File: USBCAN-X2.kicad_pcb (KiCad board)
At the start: 2 copper layers, 73 x 40.5 mm, 29 parts, among them J1 USB_B, J2 Screw_Terminal_01x08, J3 Conn_01x02_Pin, J4 Conn_02x05_Odd_Even, J5 Conn_01x02_Pin, J6 Conn_01x02_Pin, U1 STM32G491CETx, U2 LM2936-3.3, U3 MCP2542FDxMF, U4 MCP2542FDxMF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

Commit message: Update
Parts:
- added D3: LED, LED_SMD:LED_0603_1608Metric, F.Cu at (167.5, 119.1)
- added R7: 330, Resistor_SMD:R_0603_1608Metric, F.Cu at (163.0, 113.5)
- U2: footprint Package_TO_SOT_SMD:TO-252-3_TabPin2 -> Package_TO_SOT_SMD:SOT-223-3_TabPin2
- U3, U4: footprint Package_DFN_QFN:DFN-8-1EP_3x3mm_P0.65mm_EP1.55x2.4mm -> Package_SO:SOIC-8-1EP_3.9x4.9mm_P1.27mm_EP2.29x3mm
- moved J5 16.0 mm to (173.2, 107.5)
- moved J6 15.0 mm to (173.3, 99.5)
- moved J4 12.8 mm to (135.8, 119.8)
- moved R2 12.0 mm to (157.3, 113.5), turned to 0 degrees
- moved R5 11.8 mm to (178.8, 103.3)
- moved R1 11.7 mm to (148.0, 113.5), turned to 180 degrees
- moved D2 10.1 mm to (157.5, 119.0)
- moved J3 10.1 mm to (141.8, 112.4), turned to 90 degrees
- moved C2 9.78 mm to (145.8, 96.0)
- moved C1 9.55 mm to (143.3, 106.0)
- moved C10 9.02 mm to (159.8, 100.0)
- moved C3 9.02 mm to (157.8, 106.5)
- moved C4 9.02 mm to (149.8, 96.0)
- moved C7 9.02 mm to (152.8, 110.5)
- moved J1 9.02 mm to (137.1, 106.2)
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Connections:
- U1 pad 10: unconnected-(U1-PA2-Pad10) -> /LED_PA2
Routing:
- net GND: track 0.00 -> 244.7 mm, vias 0 -> 1
- net 3.3V: track 0.00 -> 154.4 mm, vias 0 -> 5
- net 5V: track 0.00 -> 79.7 mm, vias 0 -> 3
- net CAN1_RX: track 0.00 -> 62.3 mm, vias 0 -> 1
- net CAN2_P: track 63.2 -> 15.6 mm
- net CAN2_RX: track 0.00 -> 41.4 mm, vias 0 -> 2
- net SWDCLK: track 0.00 -> 33.6 mm
- net CAN2_TX: track 0.00 -> 32.9 mm, vias 0 -> 2
- net CAN1_TX: track 0.00 -> 32.1 mm, vias 0 -> 2
- net SWDIO: track 0.00 -> 29.8 mm, vias 0 -> 2
- net /LED_PA0: track 0.00 -> 22.8 mm, vias 0 -> 2
- net CAN2_N: track 34.3 -> 14.4 mm
- net Net-(J2-Pin_4): track 34.4 -> 14.8 mm
- net /LED_PA2: track 0.00 -> 18.7 mm, vias 0 -> 2
- net /LED_PA1: track 0.00 -> 13.9 mm, vias 0 -> 2
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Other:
- board size 73 x 40.5 mm -> 65 x 40 mm
- board text added: "USBCAN-X2"

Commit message: Update
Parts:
- C10, C9: value 0.1uF -> 18pF
- C5: value 10uF -> 15uF
- C6, C8: value C -> 0.1uF
- D1: value LED -> LED Green
- D2: value LED -> LED Blue
- D3: value LED -> LED Red
- J4: footprint Samtect:CON10_2X5_DUK_FTSH_SAI -> Samtect:CON10_2X5_DUK_FTSH_SAI-M
- Y1: value Crystal_Small -> 25MHz
- moved C6 1.40 mm to (166.1, 94.9)
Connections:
- U1 pad 33: USB_M -> USB_N
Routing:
- net GND: track 244.7 -> 228.2 mm, vias 1 -> 6
- net USB_N: track 0.00 -> 12.3 mm
- net CAN2_N: track 14.4 -> 24.3 mm, vias 0 -> 1
- net 5V: track 79.7 -> 76.0 mm
- net CAN1_N: track 28.6 -> 26.6 mm
- net SWDIO: track 29.8 -> 31.3 mm
- net 3.3V: track 154.4 -> 155.8 mm
- net CAN1_P: track 25.5 -> 26.1 mm
- net Net-(J2-Pin_8): track 25.2 -> 25.8 mm
- net USB_P: track 11.8 -> 12.3 mm
- added copper zone on B.Cu, net GND
- added copper zone on F.Cu, net GND

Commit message: Created PDF's
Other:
- board text added: "REV 1"
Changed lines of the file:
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@@
 		(tags "USB B receptacle horizontal through-hole")
 		(property "Reference" "J1"
-			(at 14.7875 -6.25 0)
+			(at 9.3875 -6.25 0)
 			(layer "F.SilkS")
 			(effects
@@
 		)
 	)
+	(gr_text "REV 1"
+		(at 180.2 88.8 0)
+		(layer "F.Cu")
+		(effects
+			(font
+				(size 1 1)
+				(thickness 0.15)
+			)
+			(justify left bottom)
+		)
+	)
 	(dimension
 		(type orthogonal)
@@
 		(name "GND")
 		(hatch edge 0.5)
+		(priority 1)
 		(connect_pads
 			(clearance 0.5)
@@
 		(name "GND")
 		(hatch edge 0.5)
-		(priority 1)
 		(connect_pads
 			(clearance 0.5)

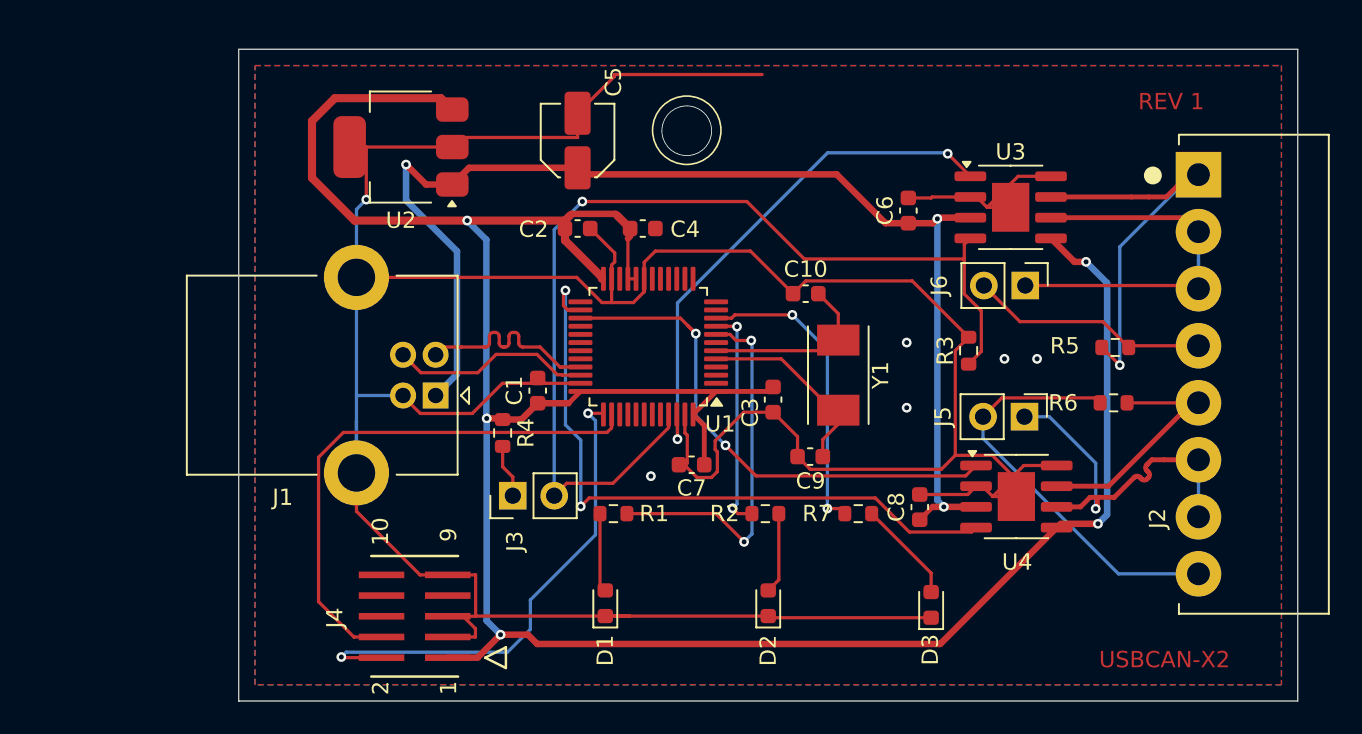
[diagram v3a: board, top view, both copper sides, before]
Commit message: Moved CAN transceiver and jumper pins. Rerouted tracks. Added 3D models to 3D folder as they are linked and not embedded.
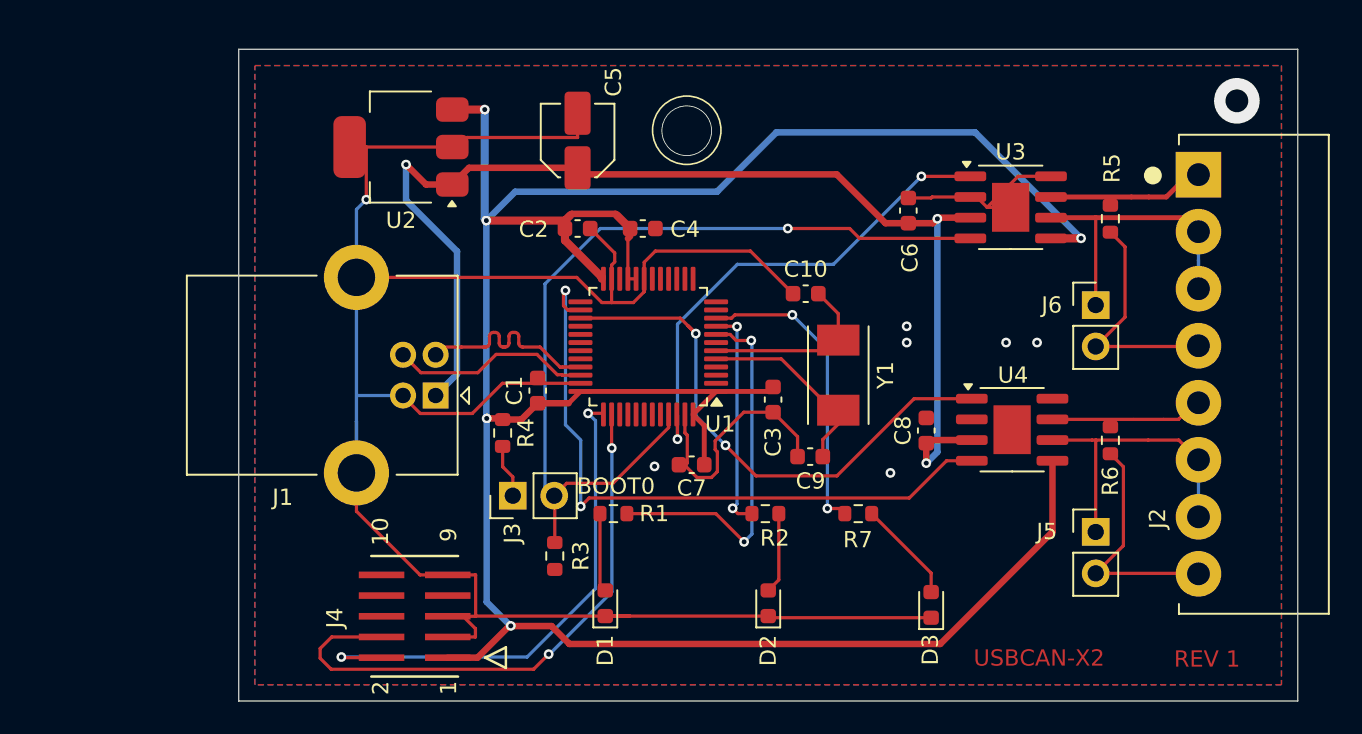
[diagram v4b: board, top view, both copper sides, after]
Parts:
- moved R3 28.4 mm to (144.4, 116.1), turned to -90 degrees
- moved J5 8.32 mm to (177.6, 114.6), turned to 0 degrees
- moved R5 7.91 mm to (178.5, 95.4), turned to -90 degrees
- moved C8 4.72 mm to (167.2, 108.4)
- moved J6 4.49 mm to (177.6, 100.7), turned to 0 degrees
- moved U4 4.11 mm to (172.5, 108.3)
- moved R6 2.31 mm to (178.5, 109.0), turned to -90 degrees
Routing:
- net GND: track 228.2 -> 170.2 mm, vias 6 -> 8
- net CAN1_P: track 26.1 -> 12.0 mm, vias 1 -> 0
- net Net-(J2-Pin_8): track 25.8 -> 14.7 mm
- net 3.3V: track 155.8 -> 164.6 mm
- net CAN1_RX: track 62.3 -> 53.9 mm
- net CAN2_P: track 15.2 -> 9.80 mm
- net CAN1_N: track 26.6 -> 21.5 mm
- net CAN2_N: track 24.3 -> 19.6 mm, vias 1 -> 0
- net SWDCLK: track 33.6 -> 36.5 mm, vias 0 -> 2
- net 5V: track 76.0 -> 73.7 mm
- net CAN1_TX: track 32.2 -> 30.5 mm
- net CAN2_TX: track 32.9 -> 34.3 mm
- net SWDIO: track 31.3 -> 32.2 mm
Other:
- board text added: "0"
- board text added: "0 mm"
- board text added: "0.01 mm"
- board text added: "0.02"
- board text added: "0.035 mm"
- board text added: "1"
- board text added: "1.51 mm"
- board text added: "3.3"
- board text added: "4.5"
- board text added: "B.Cu"
- board text added: "B.Mask"
- board text added: "B.Paste"
- board text added: "B.Silkscreen"
- board text added: "BOOT0"
- board text added: "Bottom Silk Screen"
- board text added: "Bottom Solder Mask"
- board text added: "Bottom Solder Paste"
- board text added: "Color"
- board text added: "Dielectric"
- board text added: "Epsilon R"
- board text added: "F.Cu"
- board text added: "F.Mask"
- board text added: "F.Paste"
- board text added: "F.Silkscreen"
- board text added: "FR4"
- board text added: "Layer Name"
- board text added: "Loss Tangent"
- board text added: "Material"
- board text added: "Not specified"
- board text added: "Thickness (mm)"
- board text added: "Top Silk Screen"
- board text added: "Top Solder Mask"
- board text added: "Top Solder Paste"
- board text added: "Type"
- board text added: "copper"
- board text added: "core"

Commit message: Added an alternative 4-pin debug header
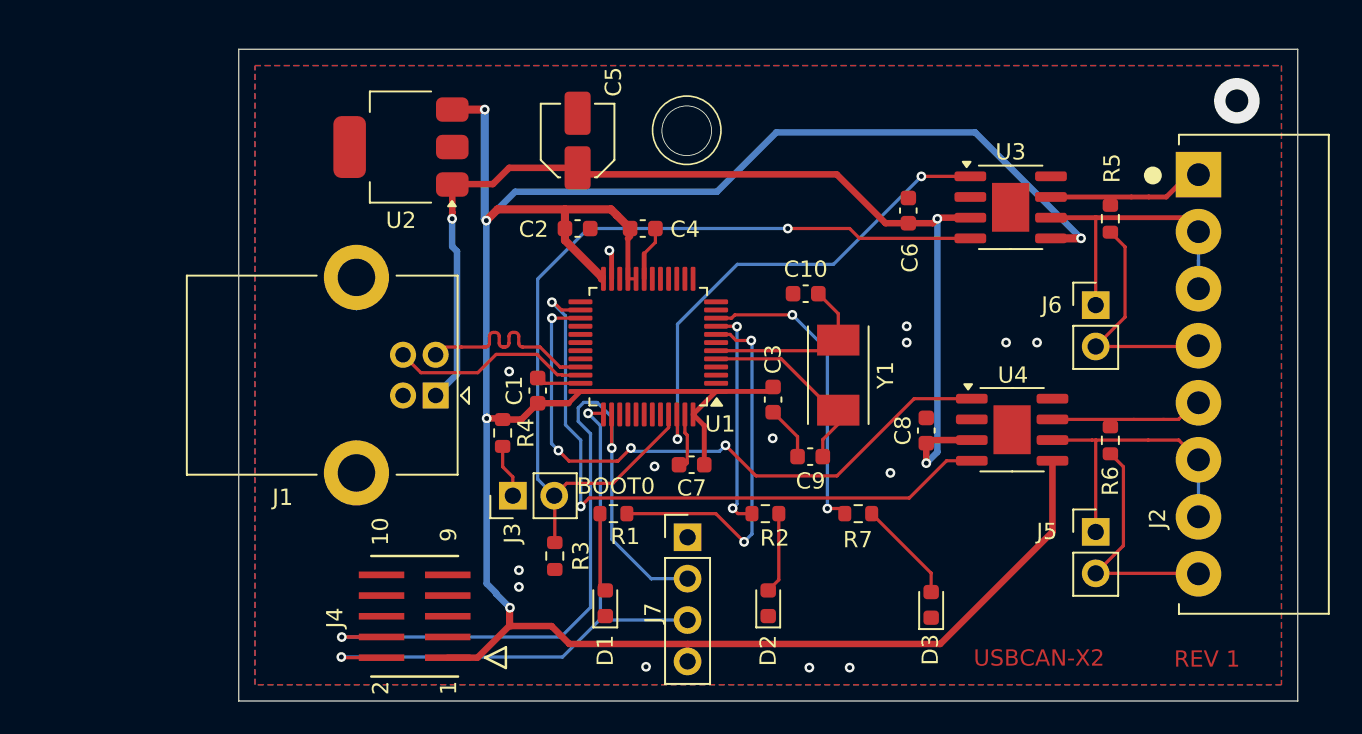
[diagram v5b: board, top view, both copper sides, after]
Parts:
- added J7: Alternative Debug Connector, Connector_PinHeader_2.54mm:PinHeader_1x04_P2.54mm_Vertical, F.Cu at (152.6, 115.0)
- D1: value LED Green -> LED Red
- D2: value LED Blue -> LED Green
- D3: value LED Red -> LED Blue
- J3: value Conn_01x02_Pin -> BOOT0
- J4: value Conn_02x05_Odd_Even -> SWD Debug
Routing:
- net GND: track 170.2 -> 20.5 mm, vias 8 -> 15
- net SWDCLK: track 36.5 -> 49.6 mm
- net SWDIO: track 32.2 -> 39.1 mm
- net 5V: track 73.7 -> 68.0 mm
- net CAN2_TX: track 34.3 -> 39.0 mm, vias 2 -> 4
- net 3.3V: track 164.6 -> 167.6 mm
- net CAN1_RX: track 53.9 -> 54.7 mm
- net CAN2_RX: track 41.1 -> 40.4 mm

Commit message: Add pull-up to NRST
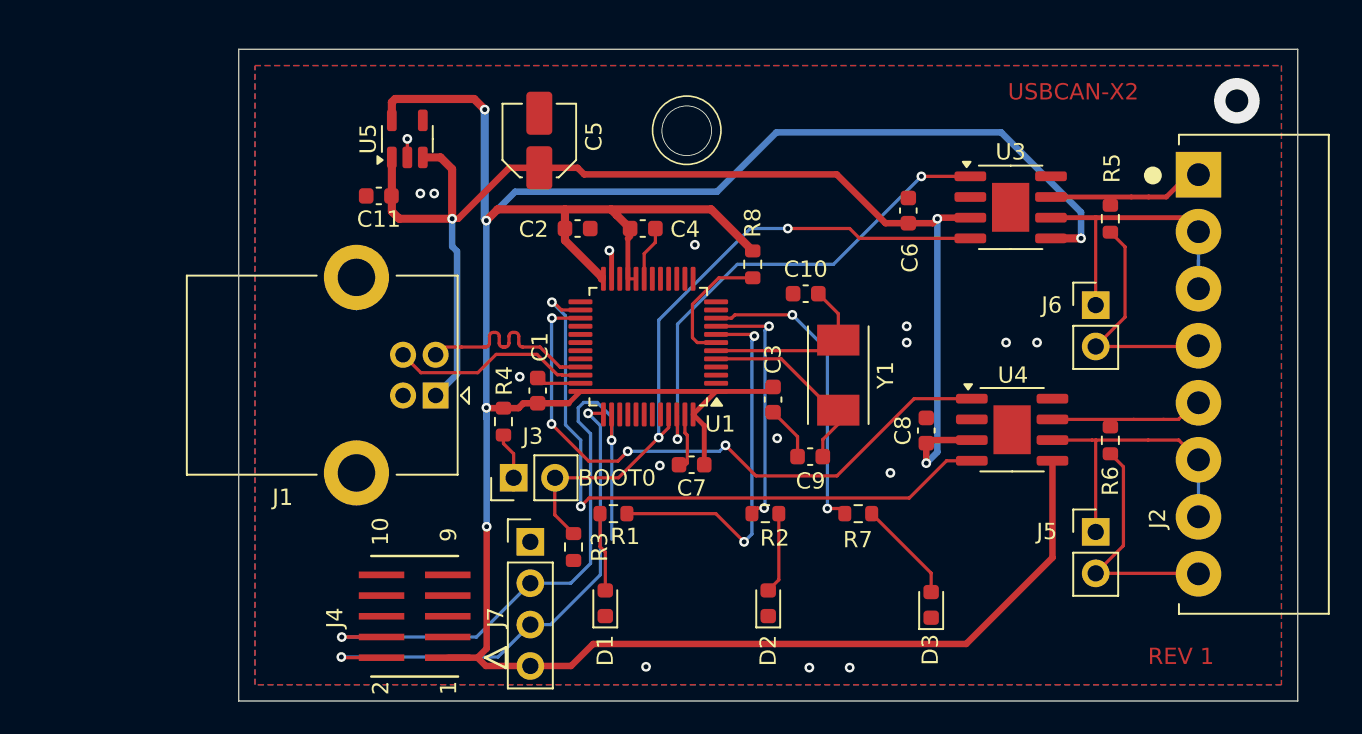
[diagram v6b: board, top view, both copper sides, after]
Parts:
- removed U2: LM2936-3.3, Package_TO_SOT_SMD:SOT-223-3_TabPin2
- added C11: 0.1uF, Capacitor_SMD:C_0603_1608Metric, F.Cu at (133.6, 94.0)
- added R8: 10K, Resistor_SMD:R_0603_1608Metric, F.Cu at (156.6, 98.2)
- added U5: ST730M33R, Package_TO_SOT_SMD:SOT-23-5, F.Cu at (135.3, 90.5)
- moved J7 9.65 mm to (142.9, 115.2)
- moved C5 2.35 mm to (143.4, 90.6)
- moved R3 1.27 mm to (145.6, 115.5)
- moved J3 1.10 mm to (141.9, 111.3)
- moved R4 0.70 mm to (141.2, 107.8)
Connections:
- U1 pad 7: unconnected-(U1-PG10-Pad7) -> Net-(U1-PG10)
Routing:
- net 3.3V: track 167.6 -> 184.3 mm
- net CAN1_RX: track 54.7 -> 42.3 mm, vias 1 -> 2
- net 5V: track 68.0 -> 79.1 mm
- net Net-(U1-PG10): track 0.00 -> 8.00 mm
- net SWDCLK: track 49.6 -> 41.9 mm
- net SWDIO: track 39.1 -> 32.1 mm
- net /LED_PA1: track 13.9 -> 15.5 mm
- net CAN2_TX: track 39.0 -> 38.1 mm
- net GND: track 20.5 -> 21.3 mm, vias 15 -> 17

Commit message: Clean some tracks up.
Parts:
- J5, J6: value Conn_01x02_Pin -> 2-pin header
- moved R1 3.90 mm to (151.9, 113.4), turned to 0 degrees
- moved R7 3.78 mm to (166.8, 113.5)
- moved R8 3.06 mm to (159.6, 98.5)
- moved R3 2.90 mm to (147.5, 113.4), turned to 0 degrees
- moved J5 2.45 mm to (177.6, 117.1), turned to 180 degrees
- moved C10 2.09 mm to (161.8, 99.4), turned to 90 degrees
- moved J6 1.98 mm to (177.5, 102.7), turned to 180 degrees
- moved C3 0.89 mm to (156.9, 106.8)
- moved C2 0.65 mm to (145.2, 96.0), turned to 180 degrees
- moved J3 0.40 mm to (141.9, 110.9)
- moved R4 0.35 mm to (141.3, 107.5)
- moved C7 0.20 mm to (152.8, 110.3)
- moved R5 0.08 mm to (178.5, 95.3)
- turned D1 to -90 degrees
- turned D2 to -90 degrees
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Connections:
- D1 pad 1: GND -> Net-(D1-K)
- D1 pad 2: Net-(D1-A) -> 3.3V
- D2 pad 1: GND -> Net-(D2-K)
- D2 pad 2: Net-(D2-A) -> 3.3V
- D3 pad 1: GND -> Net-(D3-K)
- D3 pad 2: Net-(D3-A) -> 3.3V
- J2 pad 3: CAN1_N -> unconnected-(J2-Pin_3-Pad3)
- J2 pad 4: Net-(J2-Pin_4) -> GND
- J2 pad 7: CAN2_N -> unconnected-(J2-Pin_7-Pad7)
- J2 pad 8: Net-(J2-Pin_8) -> GND
- J5 pad 2: Net-(J2-Pin_8) -> Net-(J5-Pin_2)
- J6 pad 2: Net-(J2-Pin_4) -> Net-(J6-Pin_2)
- R1 pad 1: /LED_PA0 -> Net-(D1-K)
- R1 pad 2: Net-(D1-A) -> /LED_PA0
- R2 pad 1: /LED_PA1 -> Net-(D2-K)
- R2 pad 2: Net-(D2-A) -> /LED_PA1
- R5 pad 2: Net-(J2-Pin_4) -> Net-(J6-Pin_2)
- R6 pad 2: Net-(J2-Pin_8) -> Net-(J5-Pin_2)
- R7 pad 1: /LED_PA2 -> Net-(D3-K)
- R7 pad 2: Net-(D3-A) -> /LED_PA2
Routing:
- net 3.3V: track 184.3 -> 210.0 mm, vias 5 -> 9
- net Net-(J2-Pin_8): track 14.7 -> 0.00 mm
- net Net-(J2-Pin_4): track 14.5 -> 0.00 mm
- net SWDCLK: track 41.9 -> 29.7 mm, vias 2 -> 3
- net /LED_PA0: track 23.2 -> 15.8 mm
- net Net-(D1-K): track 0.00 -> 6.69 mm
- net Net-(D3-A): track 6.32 -> 0.00 mm
- net /LED_PA2: track 18.7 -> 24.3 mm
- net Net-(D3-K): track 0.00 -> 5.44 mm
- net Net-(D2-K): track 0.00 -> 5.13 mm
- net Net-(J5-Pin_2): track 0.00 -> 5.08 mm
- net Net-(D2-A): track 4.98 -> 0.00 mm
- net Net-(D1-A): track 4.85 -> 0.00 mm
- net Net-(J6-Pin_2): track 0.00 -> 4.40 mm
- net /LED_PA1: track 15.5 -> 17.8 mm
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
